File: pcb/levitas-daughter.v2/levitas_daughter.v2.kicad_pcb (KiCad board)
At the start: 2 copper layers, 50.8 x 50.8 mm, 8 parts, among them J1 Conn_01x16_Pin, J2 Conn_01x16_Pin, J3 Conn_01x16_Pin, J4 Conn_01x16_Pin

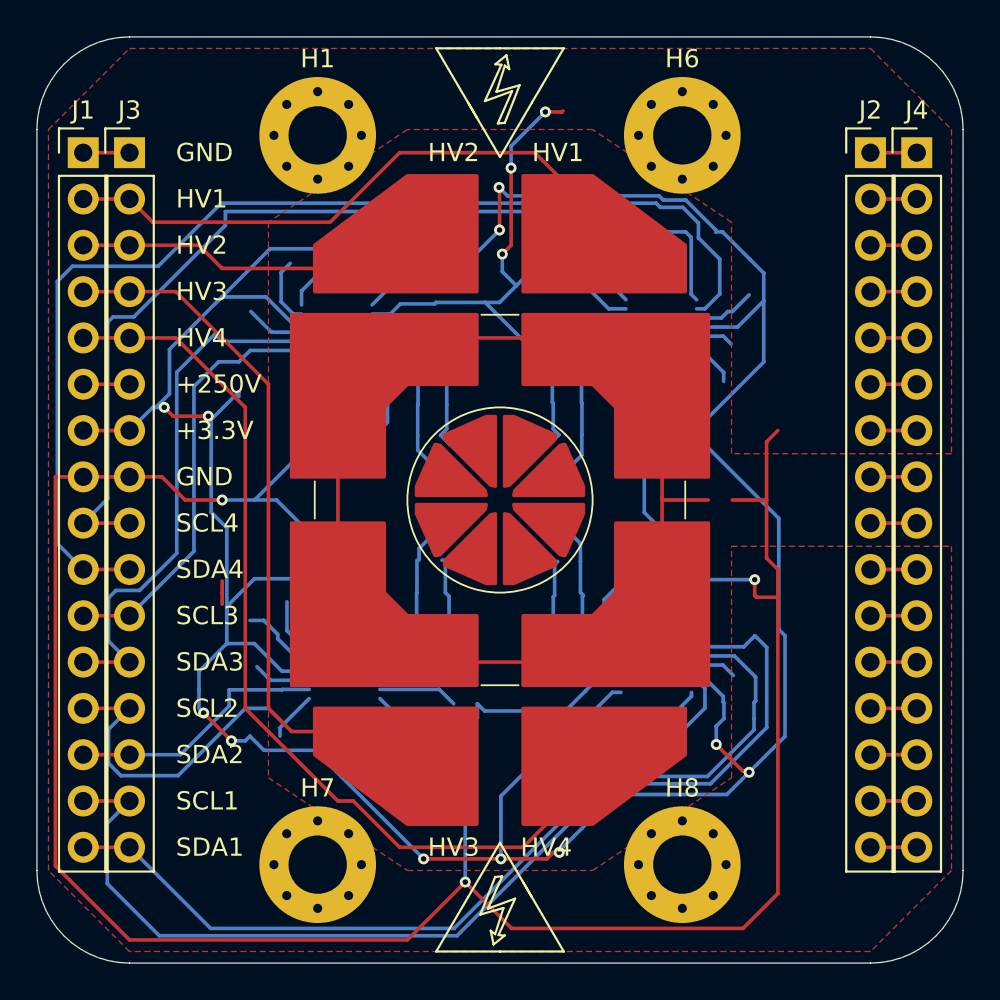
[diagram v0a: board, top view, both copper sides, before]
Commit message: This is the design for the daughter board without capacitance sensors
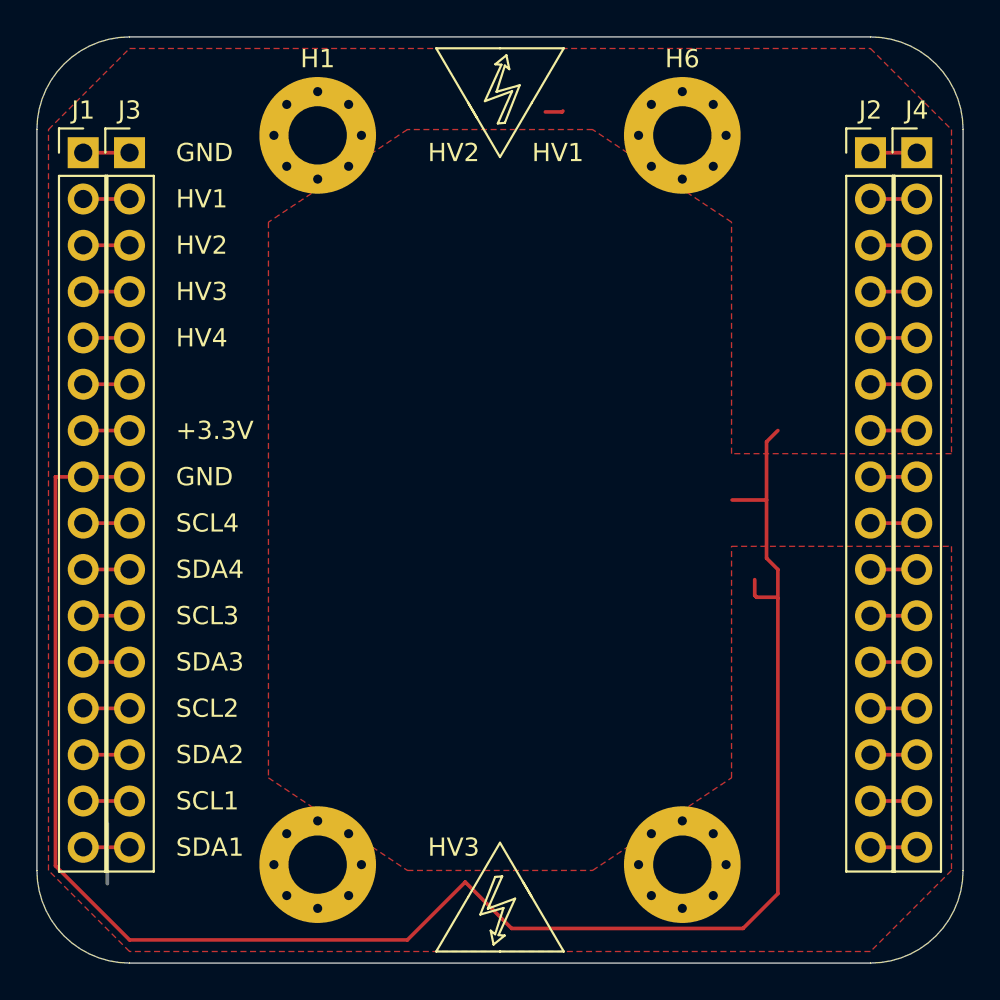
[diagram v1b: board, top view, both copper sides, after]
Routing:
- net +3.3V: track 197.3 -> 2.54 mm, vias 11 -> 0
- net GND: track 280.3 -> 103.4 mm, vias 6 -> 0
- net (no net): track 150.9 -> 0.00 mm
- net SDA4: track 62.3 -> 2.54 mm
- net SCL1: track 58.7 -> 5.86 mm
- net SCL4: track 53.2 -> 2.54 mm
- net Net-(J1-Pin_5): track 51.7 -> 2.54 mm
- net SDA1: track 50.1 -> 2.54 mm
- net Net-(J1-Pin_4): track 37.6 -> 2.54 mm
- net Net-(J1-Pin_2): track 33.2 -> 2.54 mm
- net SDA3: track 29.1 -> 2.54 mm
- net SCL3: track 23.3 -> 2.54 mm
- net SCL2: track 20.5 -> 2.54 mm
- net Net-(J1-Pin_3): track 17.7 -> 2.54 mm
- net SDA2: track 14.4 -> 2.54 mm
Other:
- board text removed: "+250V"

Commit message: v2 without copper layer, without capacitance sensors
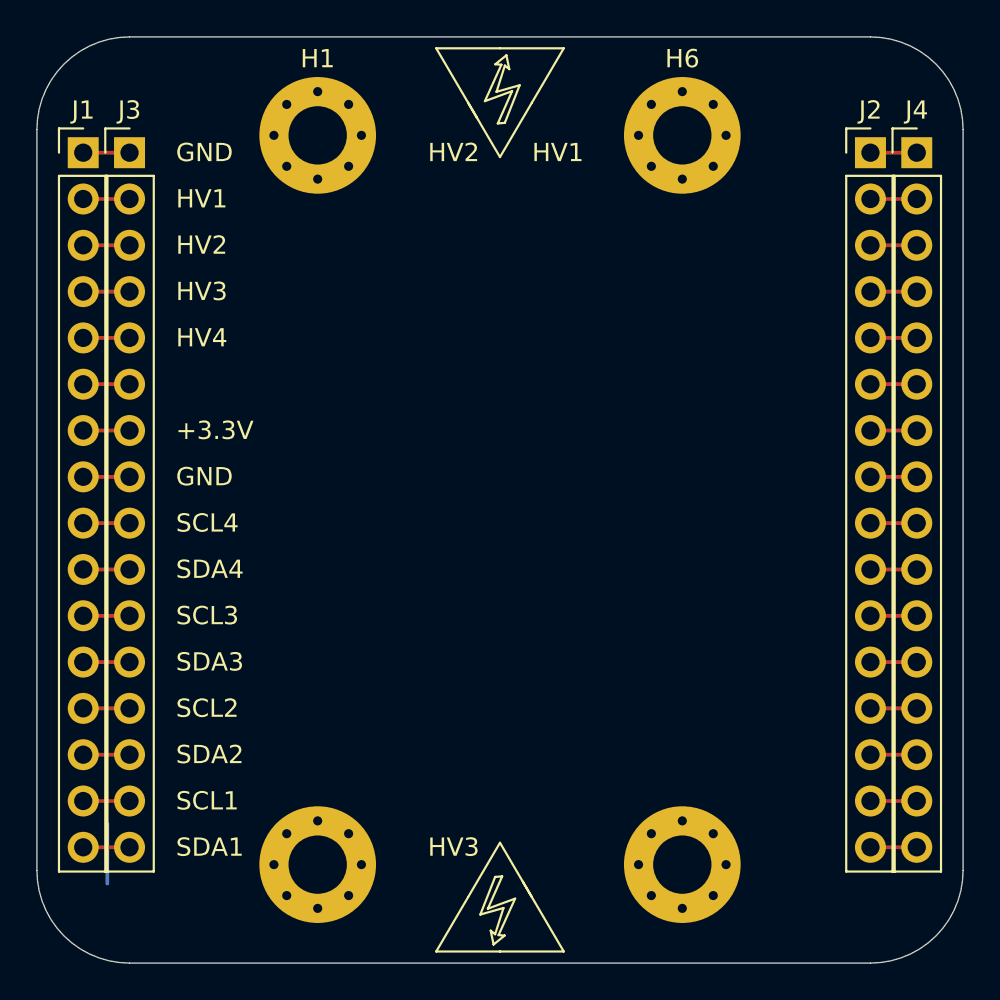
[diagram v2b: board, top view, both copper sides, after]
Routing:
- net GND: track 103.4 -> 5.08 mm
- removed copper zone on F.Cu, net GND
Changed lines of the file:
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@@
-	)
-	(segment
-		(start 120.396 108.966)
-		(end 120.396 87.63)
-		(width 0.2)
-		(layer "F.Cu")
-		(net 8)
-	)
-	(segment
-		(start 159.4 85.71)
-		(end 160.02 85.09)
-		(width 0.2)
-		(layer "F.Cu")
-		(net 8)
-	)
-	(segment
-		(start 157.51 88.9)
-		(end 159.4 88.9)
-		(width 0.2)
-		(layer "F.Cu")
-		(net 8)
-	)
-	(segment
-		(start 158.8516 94.234)
-		(end 159.9692 94.234)
-		(width 0.2)
-		(layer "F.Cu")
-		(net 8)
-	)
-	(segment
-		(start 159.4 88.9)
-		(end 159.4 85.71)
-		(width 0.2)
-		(layer "F.Cu")
-		(net 8)
-	)
-	(segment
-		(start 147.2692 67.6148)
-		(end 148.1836 67.6148)
-		(width 0.2)
-		(layer "F.Cu")
-		(net 8)
-	)
-	(segment
-		(start 139.7 113.03)
-		(end 124.46 113.03)
-		(width 0.2)
-		(layer "F.Cu")
-		(net 8)
-	)
-	(segment
-		(start 158.11 112.4)
-		(end 145.42 112.4)
-		(width 0.2)
-		(layer "F.Cu")
-		(net 8)
-	)
-	(segment
-		(start 145.42 112.4)
-		(end 142.875 109.855)
-		(width 0.2)
-		(layer "F.Cu")
-		(net 8)
-	)
-	(segment
-		(start 158.75 93.2688)
-		(end 158.75 94.1324)
-		(width 0.2)
-		(layer "F.Cu")
-		(net 8)
-	)
-	(segment
-		(start 159.4 92.09)
-		(end 160.02 92.71)
-		(width 0.2)
-		(layer "F.Cu")
-		(net 8)
-	)
-	(segment
-		(start 142.875 109.855)
-		(end 139.7 113.03)
-		(width 0.2)
-		(layer "F.Cu")
-		(net 8)
-	)
-	(segment
-		(start 120.396 87.63)
-		(end 121.92 87.63)
-		(width 0.2)
-		(layer "F.Cu")
-		(net 8)
-	)
-	(segment
-		(start 160.02 94.2848)
-		(end 160.02 110.49)
-		(width 0.2)
-		(layer "F.Cu")
-		(net 8)
 	)
 	(segment
@@
 	)
 	(segment
-		(start 158.75 94.1324)
-		(end 158.8516 94.234)
-		(width 0.2)
-		(layer "F.Cu")
-		(net 8)
-	)
-	(segment
-		(start 159.9692 94.234)
-		(end 160.02 94.2848)
-		(width 0.2)
-		(layer "F.Cu")
-		(net 8)
-	)
-	(segment
-		(start 160.02 92.71)
-		(end 160.02 94.2848)
-		(width 0.2)
-		(layer "F.Cu")
-		(net 8)
-	)
-	(segment
-		(start 124.46 113.03)
-		(end 120.396 108.966)
-		(width 0.2)
-		(layer "F.Cu")
-		(net 8)
-	)
-	(segment
-		(start 148.1836 67.6148)
-		(end 148.2344 67.564)
-		(width 0.2)
-		(layer "F.Cu")
-		(net 8)
-	)
-	(segment
-		(start 159.4 88.9)
-		(end 159.4 92.09)
-		(width 0.2)
-		(layer "F.Cu")
-		(net 8)
-	)
-	(segment
 		(start 121.92 69.85)
 		(end 124.46 69.85)
-		(width 0.2)
-		(layer "F.Cu")
-		(net 8)
-	)
-	(segment
-		(start 160.02 110.49)
-		(end 158.11 112.4)
 		(width 0.2)
 		(layer "F.Cu")
@@
 		(net 31)
 	)
-	(zone
-		(net 8)
-		(net_name "GND")
-		(layer "F.Cu")
-		(hatch edge 0.5)
-		(connect_pads
-			(clearance 0.5)
-		)
-		(min_thickness 0.25)
-		(filled_areas_thickness no)
-		(fill yes
-			(thermal_gap 0.5)
-			(thermal_bridge_width 0.5)
-		)
-		(polygon
-			(pts
-				(xy 132.08 104.14) (xy 139.7 109.22) (xy 149.86 109.22) (xy 157.48 104.14) (xy 157.48 91.44) (xy 169.545 91.44)
-				(xy 169.545 109.22) (xy 165.1 113.665) (xy 124.46 113.665) (xy 120.015 109.22) (xy 120.015 68.58)
-				(xy 124.46 64.135) (xy 165.1 64.135) (xy 169.545 68.58) (xy 169.545 86.36) (xy 157.48 86.36) (xy 157.48 73.66)
-				(xy 149.86 68.58) (xy 139.7 68.58) (xy 132.08 73.66)
-			)
-		)
-	)
 	(group ""
